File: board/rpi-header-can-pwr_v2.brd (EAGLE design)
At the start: 87 x 56.5 mm, 64 parts, among them J1 U.FL, U1 MCP2515, U2 ADS1015, U3 BME280, U4 RFM69HCW, X2 RASPI_BOARD_B+#_E3

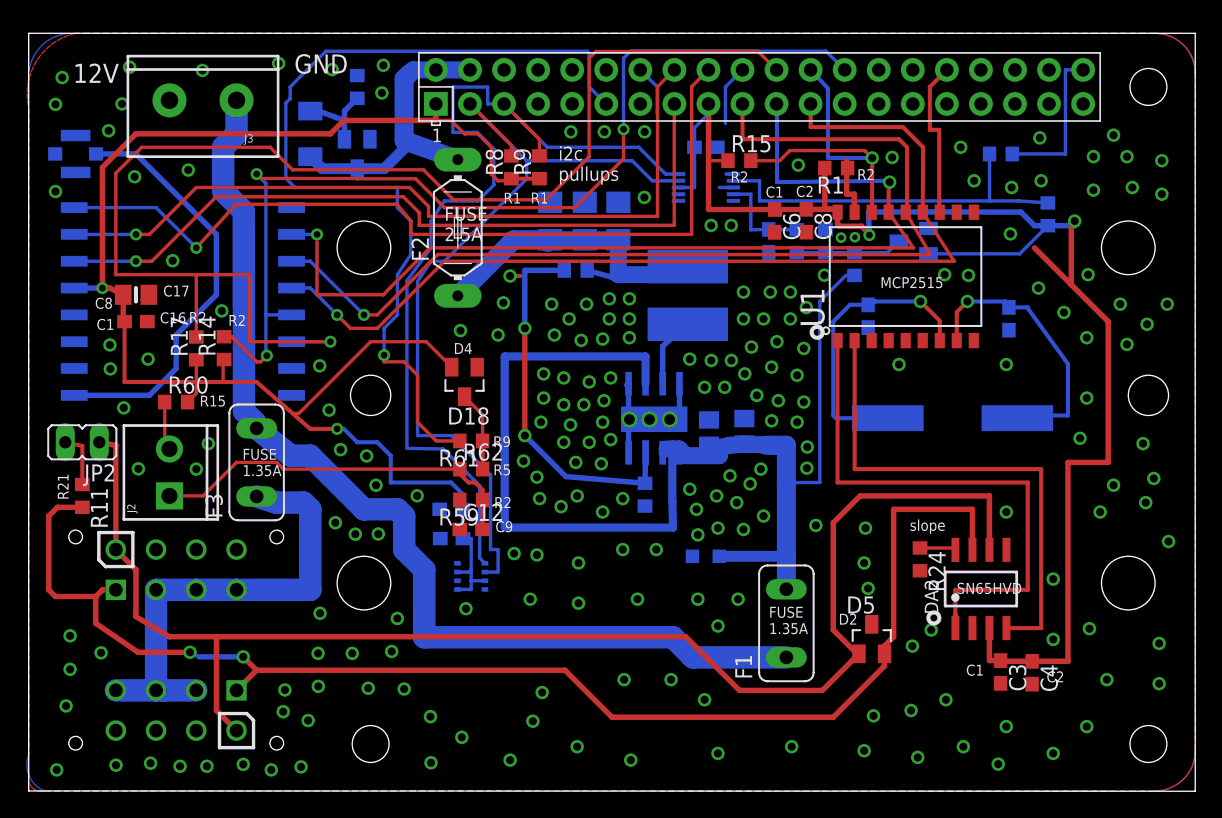
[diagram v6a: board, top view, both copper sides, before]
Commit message: fan support
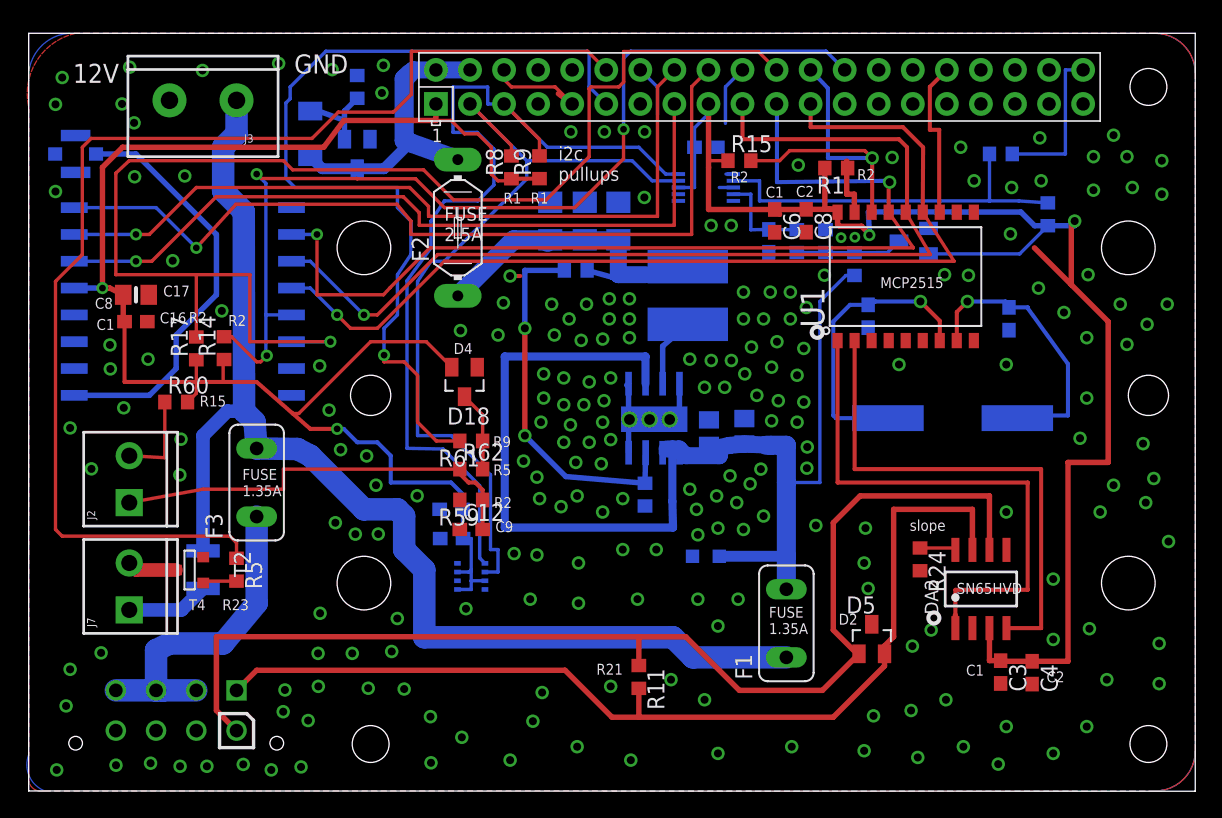
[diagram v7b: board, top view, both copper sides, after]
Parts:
- removed JP2: (no value), jumper:JP1
- removed X3: (no value), con-molex-micro-fit-3_0:43045-0812
- added F4: 1210L010, polyfuse-smd_10:1210L
- added J7: (no value), SparkFun-Connectors:SCREWTERMINAL-3.5MM-2
- added R5: 500, rcl:R0603
- added T2: (no value), zetex:SOT-23
- moved R11 43.6 mm to (45.5, 8.50)
- moved J2 3.04 mm to (7.50, 21.5)
- moved F3 1.50 mm to (17.0, 23.0)
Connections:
- new net FAN_PWM: R5.1, X2.12
- new net N$13: F4.1, J7.1
- new net N$14: J7.2, T2.1
- net CAN_H: no longer X3.P$1
- net CAN_L: now also R11.1; no longer JP2.1, X3.P$5
- net CAN_PWR: no longer X3.P$2, X3.P$3, X3.P$4
- net GND: now also T2.2; no longer X3.P$6, X3.P$7, X3.P$8
- net N$12: now also R5.2, T2.3; no longer JP2.2, R11.1
- net PRE_FUSE_12V: now also F4.2
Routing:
- net FAN_PWM: track 0.00 -> 88.9 mm
- net CAN_H: track 101.7 -> 75.0 mm, vias 2 -> 0
- net CAN_L: track 106.5 -> 87.6 mm
- net PRE_FUSE_12V: track 76.7 -> 90.0 mm
- net CAN_PWR: track 35.5 -> 25.2 mm
- net GND: track 24.4 -> 32.3 mm
- net N$13: track 0.00 -> 6.16 mm
- net N$14: track 0.00 -> 3.70 mm
- net N$11: track 28.4 -> 31.7 mm
- net N$10: track 3.64 -> 6.80 mm
- net N$12: track 4.18 -> 2.54 mm
- net LORA_RST: track 97.3 -> 96.4 mm
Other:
- board text added: "FUSE 500mA"
- board text added: "GND FAN 12V MAX 0.5A"
- board text added: "R23"
- board text added: "T4"
- board text added: "TAMPER"
- board text removed: "CAN TERMI NATION"
- board text removed: "tamper"
